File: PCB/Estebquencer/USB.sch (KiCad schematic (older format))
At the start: 0 parts

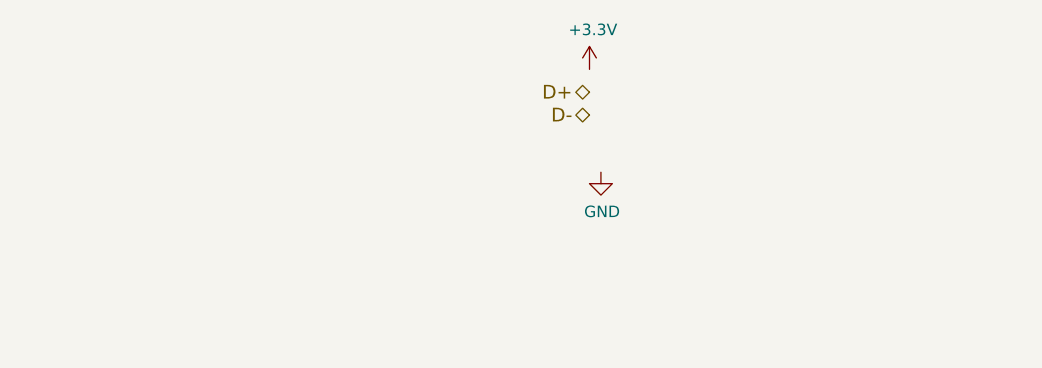
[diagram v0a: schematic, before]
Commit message: acabado módulo usb
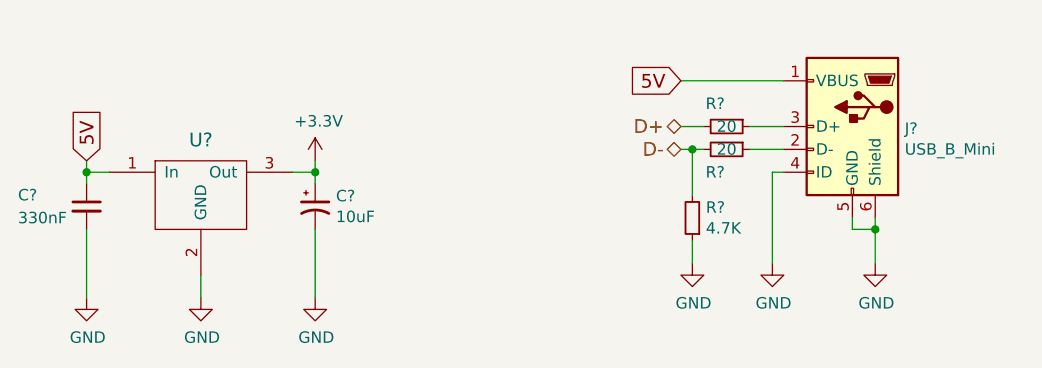
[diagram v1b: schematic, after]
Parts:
- added C?: 330nF, symbol Device:C_Small
- added C?: 10uF, symbol Device:CP1_Small
- added J?: USB_B_Mini, symbol Connector:USB_B_Mini
- added R? (x2): 20, symbol Device:R_Small
- added R?: 4.7K, symbol Device:R_Small
- added U?: LD29150, symbol libreria_proyecto:LD29150
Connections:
- net +3V3: now also C?.1, U?.3 (Out)
- net D+: now also R?.2
- net D-: now also R?.2, R?.2
- net GND: now also C?.2, C?.2, J?.4 (ID), J?.5 (GND), J?.6 (Shield), R?.1, U?.2 (GND)
- new net: J?.2 (D-), R?.1
- new net: J?.3 (D+), R?.1
- new net 5V: C?.1, J?.1 (VBUS), U?.1 (In)
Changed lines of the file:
@@
 Comment4 ""
 $EndDescr
-Text HLabel 6000 3500 0    60   BiDi ~ 0
+Text HLabel 6400 3650 0    60   BiDi ~ 0
 D+
-Text HLabel 6000 3600 0    60   BiDi ~ 0
+Text HLabel 6400 3750 0    60   BiDi ~ 0
 D-
 $Comp
+L power:GND #PWR?
+U 1 1 5F4CAB5E
+P 6450 4250
+F 0 "#PWR?" H 6450 4000 50  0001 C CNN
+F 1 "GND" H 6455 4077 50  0000 C CNN
+F 2 "" H 6450 4250 50  0001 C CNN
+F 3 "" H 6450 4250 50  0001 C CNN
+	1    6450 4250
+	1    0    0    -1
+$EndComp
+$Comp
+L libreria_proyecto:LD29150 U?
+U 1 1 5E3B2531
+P 4300 3950
+F 0 "U?" H 4300 4191 60  0000 C CNN
+F 1 "LD29150" H 4250 4200 60  0001 C CNN
+F 2 "" H 4250 4050 60  0001 C CNN
+F 3 "" H 4250 4050 60  0001 C CNN
+	1    4300 3950
+	1    0    0    -1
+$EndComp
+$Comp
 L power:+3.3V #PWR?
-U 1 1 5F4CAB27
-P 6000 3400
-F 0 "#PWR?" H 6000 3250 50  0001 C CNN
-F 1 "+3.3V" H 6015 3573 50  0000 C CNN
-F 2 "" H 6000 3400 50  0001 C CNN
-F 3 "" H 6000 3400 50  0001 C CNN
-	1    6000 3400
-	1    0    0    -1
-$EndComp
-$Comp
-L power:GND #PWR?
-U 1 1 5F4CAB5E
-P 6050 3850
-F 0 "#PWR?" H 6050 3600 50  0001 C CNN
-F 1 "GND" H 6055 3677 50  0000 C CNN
-F 2 "" H 6050 3850 50  0001 C CNN
-F 3 "" H 6050 3850 50  0001 C CNN
-	1    6050 3850
-	1    0    0    -1
-$EndComp
+U 1 1 5E3B2575
+P 4800 3800
+F 0 "#PWR?" H 4800 3650 50  0001 C CNN
+F 1 "+3.3V" H 4815 3973 50  0000 C CNN
+F 2 "" H 4800 3800 50  0001 C CNN
+F 3 "" H 4800 3800 50  0001 C CNN
+	1    4800 3800
+	1    0    0    -1
+$EndComp
+Text GLabel 3800 3800 1    60   Input ~ 0
+5V
+Text GLabel 6400 3450 0    60   Input ~ 0
+5V
+$Comp
+L Connector:USB_B_Mini J?
+U 1 1 5E3B26DC
+P 7150 3650
+F 0 "J?" H 6921 3641 50  0000 R CNN
+F 1 "USB_B_Mini" H 6921 3550 50  0000 R CNN
+F 2 "" H 7300 3600 50  0001 C CNN
+F 3 "~" H 7300 3600 50  0001 C CNN
+	1    7150 3650
+	-1   0    0    -1
+$EndComp
+$Comp
+L Device:R_Small R?
+U 1 1 5E3B2C53
+P 6600 3650
+F 0 "R?" V 6500 3600 50  0000 C CNN
+F 1 "20" V 6600 3650 50  0000 C CNN
+F 2 "" H 6600 3650 50  0001 C CNN
+F 3 "~" H 6600 3650 50  0001 C CNN
+	1    6600 3650
+	0    1    1    0
+$EndComp
+$Comp
+L Device:R_Small R?
+U 1 1 5E3B2CCD
+P 6450 4050
+F 0 "R?" H 6391 4004 50  0000 R CNN
+F 1 "4.7K" H 6391 4095 50  0000 R CNN
+F 2 "" H 6450 4050 50  0001 C CNN
+F 3 "~" H 6450 4050 50  0001 C CNN
+	1    6450 4050
+	-1   0    0    1
+$EndComp
+$Comp
+L power:GND #PWR?
+U 1 1 5E3B31EE
+P 4300 4400
+F 0 "#PWR?" H 4300 4150 50  0001 C CNN
+F 1 "GND" H 4305 4227 50  0000 C CNN
+F 2 "" H 4300 4400 50  0001 C CNN
+F 3 "" H 4300 4400 50  0001 C CNN
+	1    4300 4400
+	1    0    0    -1
+$EndComp
+$Comp
+L Device:C_Small C?
+U 1 1 5E3B3804
+P 3800 4000
+F 0 "C?" H 3500 4050 50  0000 L CNN
+F 1 "330nF" H 3500 3950 50  0000 L CNN
+F 2 "" H 3800 4000 50  0001 C CNN
+F 3 "~" H 3800 4000 50  0001 C CNN
+	1    3800 4000
+	1    0    0    -1
+$EndComp
+$Comp
+L Device:CP1_Small C?
+U 1 1 5E3B392C
+P 4800 4000
+F 0 "C?" H 4891 4046 50  0000 L CNN
+F 1 "10uF" H 4891 3955 50  0000 L CNN
+F 2 "" H 4800 4000 50  0001 C CNN
+F 3 "~" H 4800 4000 50  0001 C CNN
+	1    4800 4000
+	1    0    0    -1
+$EndComp
+Wire Wire Line
+	4300 4400 4300 4300
+Wire Wire Line
+	3800 3850 3800 3800
+Wire Wire Line
+	3900 3850 3800 3850
+Wire Wire Line
+	3800 3850 3800 3900
+Connection ~ 3800 3850
+Wire Wire Line
+	4800 3900 4800 3850
+Wire Wire Line
+	4700 3850 4800 3850
+Connection ~ 4800 3850
+Wire Wire Line
+	4800 3850 4800 3800
+$Comp
+L power:GND #PWR?
+U 1 1 5E3B46E3
+P 3800 4400
+F 0 "#PWR?" H 3800 4150 50  0001 C CNN
+F 1 "GND" H 3805 4227 50  0000 C CNN
+F 2 "" H 3800 4400 50  0001 C CNN
+F 3 "" H 3800 4400 50  0001 C CNN
+	1    3800 4400
+	1    0    0    -1
+$EndComp
+$Comp
+L power:GND #PWR?
+U 1 1 5E3B46FC
+P 4800 4400
+F 0 "#PWR?" H 4800 4150 50  0001 C CNN
+F 1 "GND" H 4805 4227 50  0000 C CNN
+F 2 "" H 4800 4400 50  0001 C CNN
+F 3 "" H 4800 4400 50  0001 C CNN
+	1    4800 4400
+	1    0    0    -1
+$EndComp
+Wire Wire Line
+	4800 4400 4800 4100
+Wire Wire Line
+	3800 4100 3800 4400
+$Comp
+L Device:R_Small R?
+U 1 1 5E3B5444
+P 6600 3750
+F 0 "R?" V 6700 3700 50  0000 C CNN
+F 1 "20" V 6600 3750 50  0000 C CNN
+F 2 "" H 6600 3750 50  0001 C CNN
+F 3 "~" H 6600 3750 50  0001 C CNN
+	1    6600 3750
+	0    1    1    0
+$EndComp
+Wire Wire Line
+	6450 3750 6400 3750
+Wire Wire Line
+	6450 3750 6450 3950
+Wire Wire Line
+	6500 3750 6450 3750
+Connection ~ 6450 3750
+Wire Wire Line
+	6400 3650 6500 3650
+Wire Wire Line
+	6700 3650 6850 3650
+Wire Wire Line
+	6850 3750 6700 3750
+Wire Wire Line
+	6850 3450 6400 3450
+$Comp
+L power:GND #PWR?
+U 1 1 5E3B62F0
+P 7250 4250
+F 0 "#PWR?" H 7250 4000 50  0001 C CNN
+F 1 "GND" H 7255 4077 50  0000 C CNN
+F 2 "" H 7250 4250 50  0001 C CNN
+F 3 "" H 7250 4250 50  0001 C CNN
+	1    7250 4250
+	1    0    0    -1
+$EndComp
+$Comp
+L power:GND #PWR?
+U 1 1 5E3B6D2E
+P 6800 4250
+F 0 "#PWR?" H 6800 4000 50  0001 C CNN
+F 1 "GND" H 6805 4077 50  0000 C CNN
+F 2 "" H 6800 4250 50  0001 C CNN
+F 3 "" H 6800 4250 50  0001 C CNN
+	1    6800 4250
+	1    0    0    -1
+$EndComp
+Wire Wire Line
+	6800 4250 6800 3850
+Wire Wire Line
+	6800 3850 6850 3850
+Wire Wire Line
+	6450 4250 6450 4150
+Wire Wire Line
+	7250 4250 7250 4100
+Wire Wire Line
+	7150 4050 7150 4100
+Wire Wire Line
+	7150 4100 7250 4100
+Connection ~ 7250 4100
+Wire Wire Line
+	7250 4100 7250 4050
 $EndSCHEMATC

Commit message: Había un pin desconectador de la matriz de LEDs
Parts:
- gave numbers to parts that had none: 7
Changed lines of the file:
@@
 $Descr A4 11693 8268
 encoding utf-8
-Sheet 9 11
+Sheet 5 11
 Title ""
 Date ""
@@
 $EndComp
 $Comp
-L libreria_proyecto:LD29150 U?
+L libreria_proyecto:LD29150 U3
 U 1 1 5E3B2531
 P 4300 3950
-F 0 "U?" H 4300 4191 60  0000 C CNN
+F 0 "U3" H 4300 4191 60  0000 C CNN
 F 1 "LD29150" H 4250 4200 60  0001 C CNN
 F 2 "" H 4250 4050 60  0001 C CNN
@@
 5V
 $Comp
-L Connector:USB_B_Mini J?
+L Connector:USB_B_Mini J9
 U 1 1 5E3B26DC
 P 7150 3650
-F 0 "J?" H 6921 3641 50  0000 R CNN
+F 0 "J9" H 6921 3641 50  0000 R CNN
 F 1 "USB_B_Mini" H 6921 3550 50  0000 R CNN
 F 2 "" H 7300 3600 50  0001 C CNN
@@
 $EndComp
 $Comp
-L Device:R_Small R?
+L Device:R_Small R6
 U 1 1 5E3B2C53
 P 6600 3650
-F 0 "R?" V 6500 3600 50  0000 C CNN
+F 0 "R6" V 6500 3600 50  0000 C CNN
 F 1 "20" V 6600 3650 50  0000 C CNN
 F 2 "" H 6600 3650 50  0001 C CNN
@@
 $EndComp
 $Comp
-L Device:R_Small R?
+L Device:R_Small R5
 U 1 1 5E3B2CCD
 P 6450 4050
-F 0 "R?" H 6391 4004 50  0000 R CNN
+F 0 "R5" H 6391 4004 50  0000 R CNN
 F 1 "4.7K" H 6391 4095 50  0000 R CNN
 F 2 "" H 6450 4050 50  0001 C CNN
@@
 $EndComp
 $Comp
-L Device:C_Small C?
+L Device:C_Small C5
 U 1 1 5E3B3804
 P 3800 4000
-F 0 "C?" H 3500 4050 50  0000 L CNN
+F 0 "C5" H 3500 4050 50  0000 L CNN
 F 1 "330nF" H 3500 3950 50  0000 L CNN
 F 2 "" H 3800 4000 50  0001 C CNN
@@
 $EndComp
 $Comp
-L Device:CP1_Small C?
+L Device:CP1_Small C6
 U 1 1 5E3B392C
 P 4800 4000
-F 0 "C?" H 4891 4046 50  0000 L CNN
+F 0 "C6" H 4891 4046 50  0000 L CNN
 F 1 "10uF" H 4891 3955 50  0000 L CNN
 F 2 "" H 4800 4000 50  0001 C CNN
@@
 	3800 4100 3800 4400
 $Comp
-L Device:R_Small R?
+L Device:R_Small R7
 U 1 1 5E3B5444
 P 6600 3750
-F 0 "R?" V 6700 3700 50  0000 C CNN
+F 0 "R7" V 6700 3700 50  0000 C CNN
 F 1 "20" V 6600 3750 50  0000 C CNN
 F 2 "" H 6600 3750 50  0001 C CNN
